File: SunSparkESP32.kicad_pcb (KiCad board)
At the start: 4 copper layers, 38.1 x 58.2 mm, 51 parts, among them J1 Conn_01x02_Pin, J2 USB_C_Receptacle_USB2.0, J3 Conn_01x03_Pin, J4 Conn_01x15_Pin, J5 Conn_01x03_Pin, J6 Conn_01x15_Pin, J7 Conn_01x01_Pin, Q1 IRLML6244TRPBF, Q2 IRLML6244TRPBF, SW1 SW_Push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

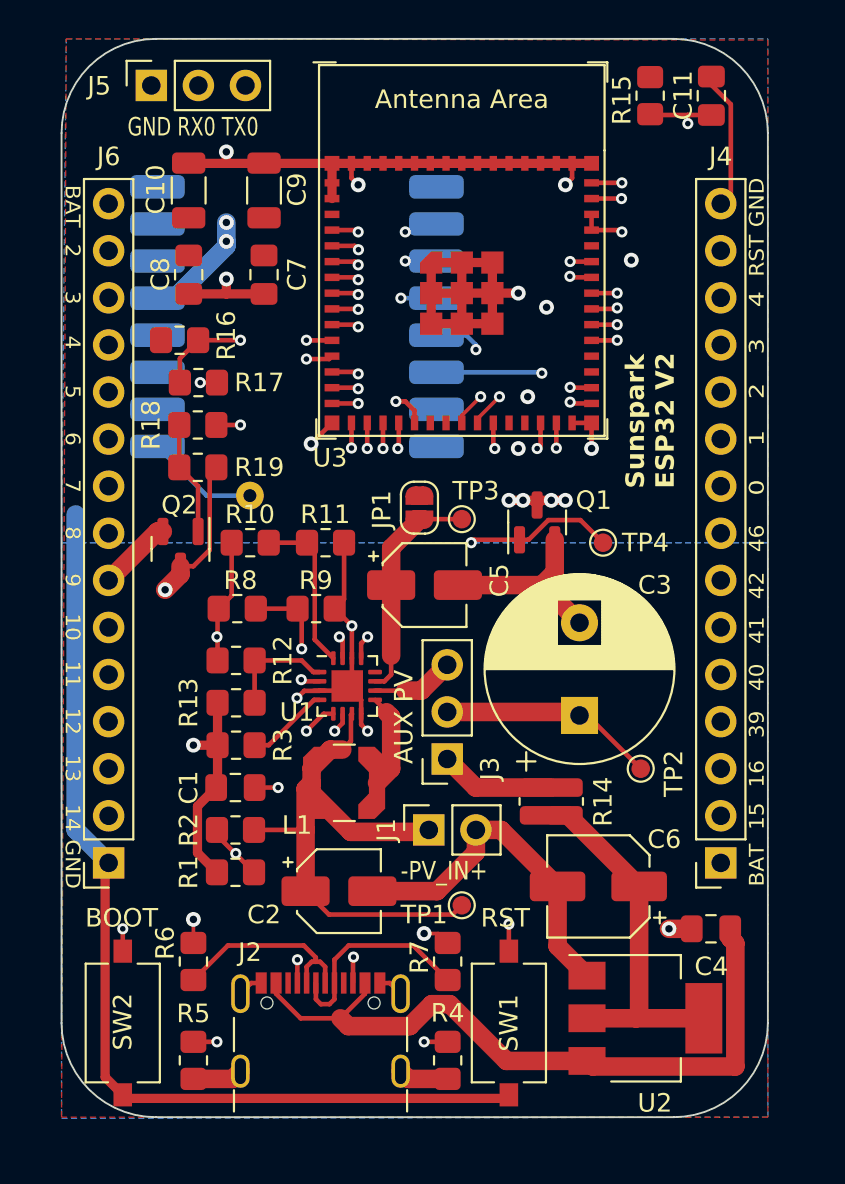
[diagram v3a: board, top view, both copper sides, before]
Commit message: Rework due to first review -Replaced electrolytic caps with low ESR ceramic ones -Routing optimizations Also added possible connection for backup battery Routed some DIOs from LoRa module on controller Updated outputs and BOM
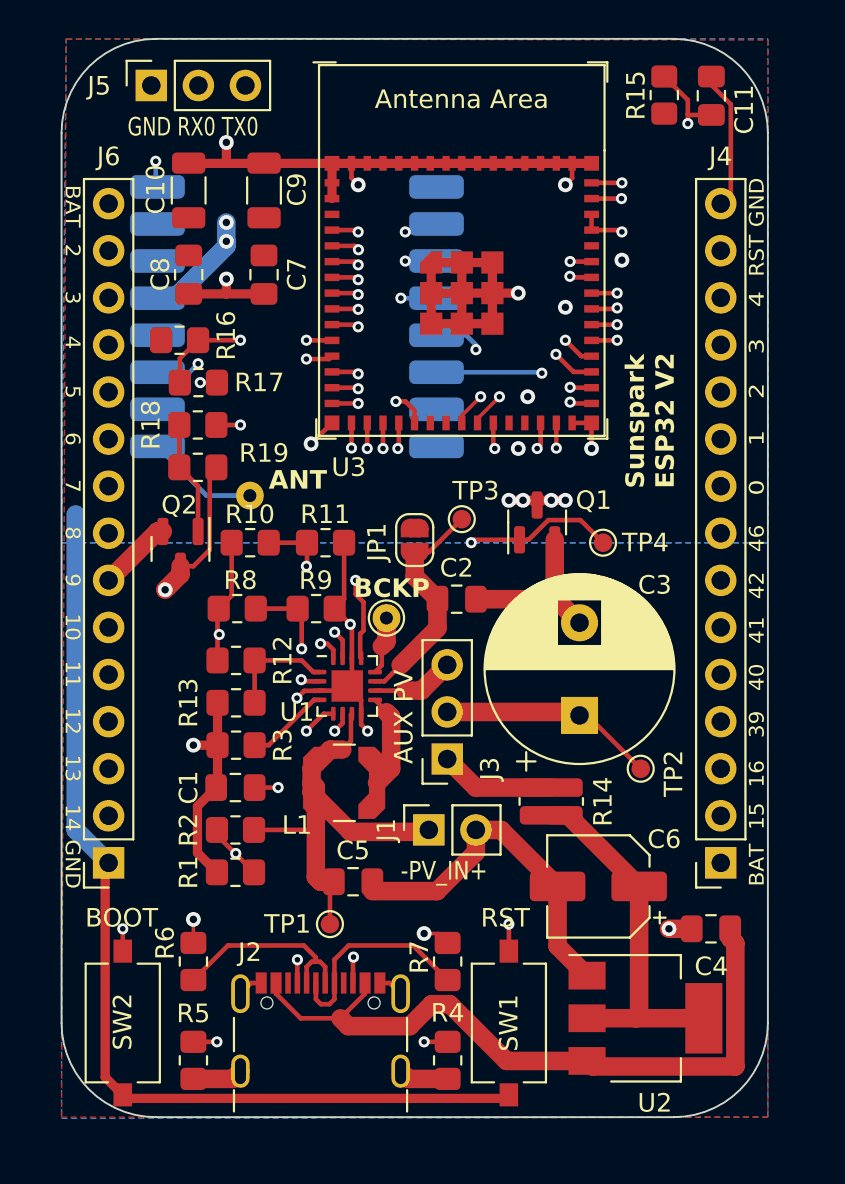
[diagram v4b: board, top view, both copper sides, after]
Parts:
- added J8: Conn_01x01_Pin, TestPoint:TestPoint_THTPad_D1.5mm_Drill0.7mm, F.Cu at (69.6, 70.6)
- C2, C5: value 4.7µ -> 4µ7; footprint Capacitor_SMD:CP_Elec_4x3 -> Capacitor_SMD:C_0805_2012Metric_Pad1.18x1.45mm_HandSolder
- moved C2 17.0 mm to (73.4, 69.6)
- moved C5 16.5 mm to (67.8, 84.8)
- moved TP1 7.18 mm to (66.5, 87.1)
- moved JP1 1.77 mm to (71.1, 66.4)
- moved R15 0.76 mm to (84.6, 42.4), turned to 90 degrees
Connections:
- C2 pad 1: Net-(J1-Pin_1) -> Net-(JP1-A)
- C5 pad 1: Net-(JP1-A) -> Net-(J1-Pin_1)
- U1 pad 12: unconnected-(U1-BACKUP-Pad12) -> Net-(J8-Pin_1)
- U3 pad 33: unconnected-(U3-GPIO37-Pad33) -> DIO3
- U3 pad 34: unconnected-(U3-GPIO38-Pad34) -> DIO2
- U4 pad 11: unconnected-(U4-DIO3-Pad11) -> DIO3
- U4 pad 16: unconnected-(U4-DIO2-Pad16) -> DIO2
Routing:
- net DIO3: track 0.00 -> 34.8 mm, vias 0 -> 2
- net DIO2: track 0.00 -> 33.0 mm, vias 0 -> 2
- net Net-(J1-Pin_1): track 30.7 -> 24.7 mm
- net Net-(J8-Pin_1): track 0.00 -> 3.17 mm
- net Net-(J5-Pin_2): track 25.1 -> 27.4 mm
- net PGOOD: track 17.7 -> 19.7 mm
- net Net-(J5-Pin_3): track 25.4 -> 27.2 mm
- net +BATT: track 14.8 -> 13.3 mm
- net rst_btn: track 81.0 -> 82.3 mm
- net GND: track 72.1 -> 71.2 mm
- net Net-(J6-Pin_10): track 17.4 -> 18.2 mm
- net GND1: track 124.7 -> 125.2 mm
- net Net-(U1-SETPG): track 8.88 -> 9.13 mm, vias 0 -> 2
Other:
- board text added: "ANT"
- board text added: "BCKP"

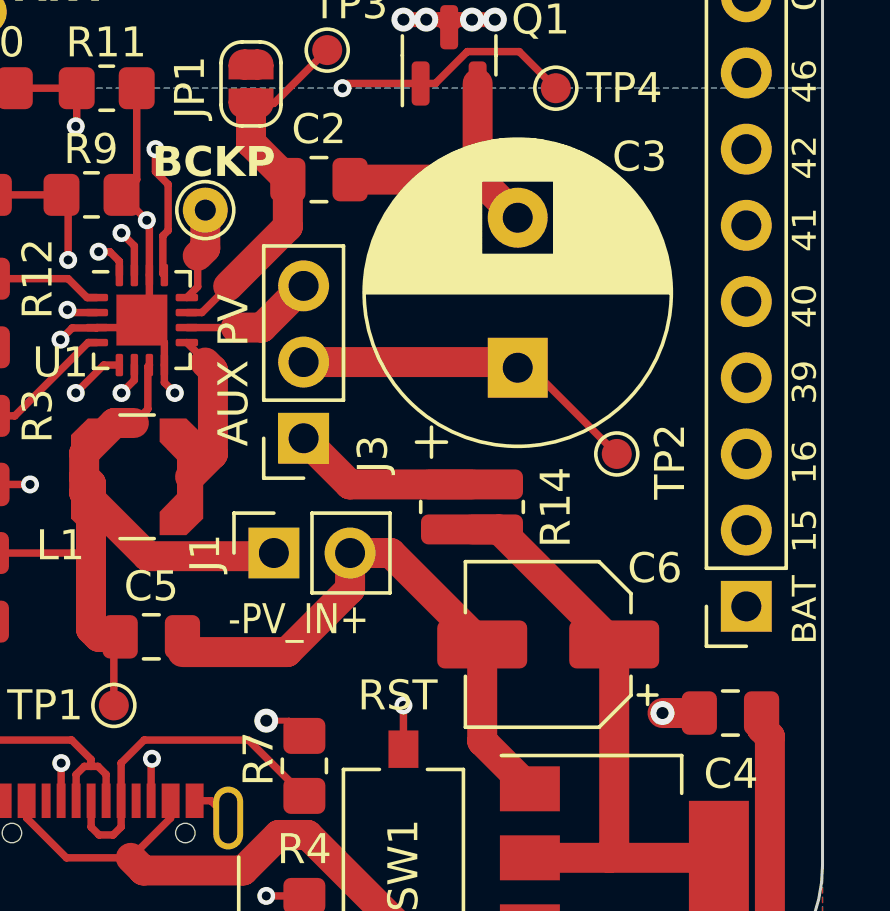
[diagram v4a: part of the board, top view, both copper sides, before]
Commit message: Finalized last review points, enhanced doc -Added Diode to prevent discharge from supercap into LDO -Updated BOM -Made readme nicer
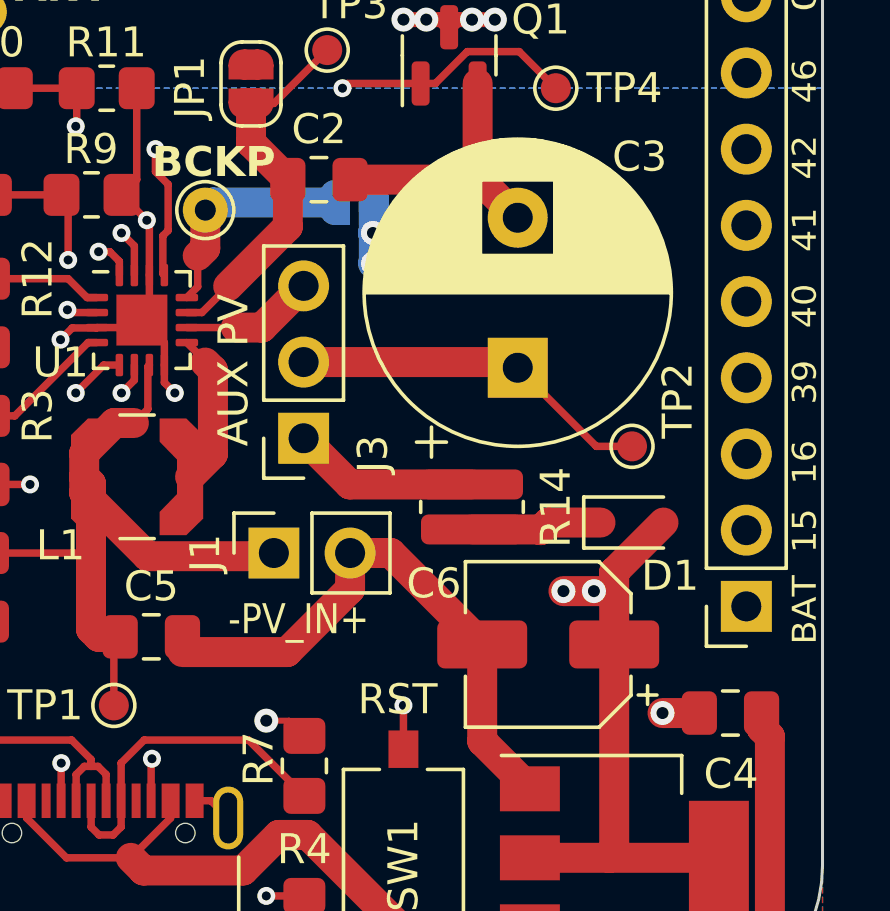
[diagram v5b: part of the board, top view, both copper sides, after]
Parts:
- added D1: D_Schottky, Diode_SMD:D_SOD-323, F.Cu at (83.8, 81.0)
- added JP2: SolderJumper_2_Open, Jumper:SolderJumper-2_P1.3mm_Open_RoundedPad1.0x1.5mm, B.Cu at (74.6, 70.4)
- moved TP2 0.57 mm to (83.8, 78.5)
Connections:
- net Net-(J8-Pin_1) renamed BCKP
- C6 pad 1: Net-(U2-VO) -> Net-(D1-A)
- R14 pad 1: Net-(U2-VO) -> Net-(D1-K)
- U2 pad 2: Net-(U2-VO) -> Net-(D1-A)
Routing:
- net Net-(D1-A): track 0.00 -> 37.6 mm, vias 0 -> 4
- net Net-(U2-VO): track 19.8 -> 0.00 mm
- net BCKP: track 3.17 -> 7.59 mm
- net Net-(D1-K): track 0.00 -> 4.40 mm
